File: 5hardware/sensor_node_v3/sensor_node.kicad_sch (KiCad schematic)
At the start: 19 parts, among them J1 Conn_01x15, J2 Conn_01x15, SW2 SW_DIP_x04, SW3 SW_Push, SW5 RotaryEncoder, U5 MCP1700x-330xxTO, U7 CH32V003F4P6

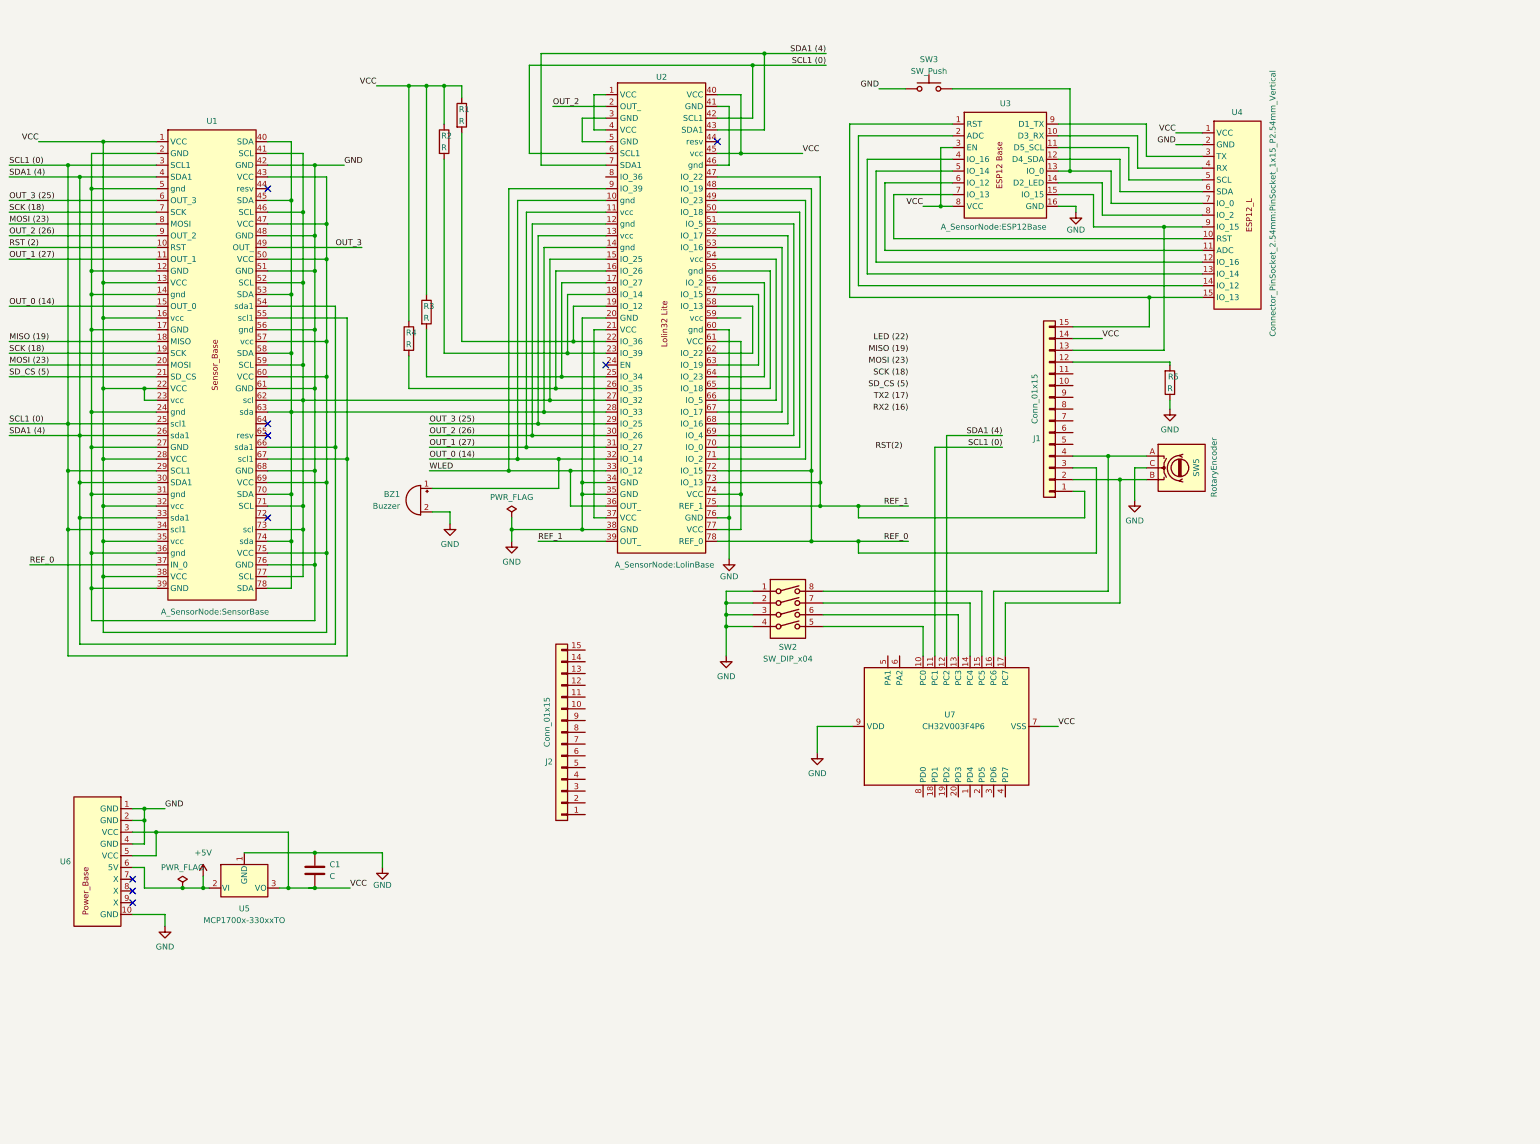
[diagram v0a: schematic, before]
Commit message: updating ESP-Mess baseboard schematic for version 3.0
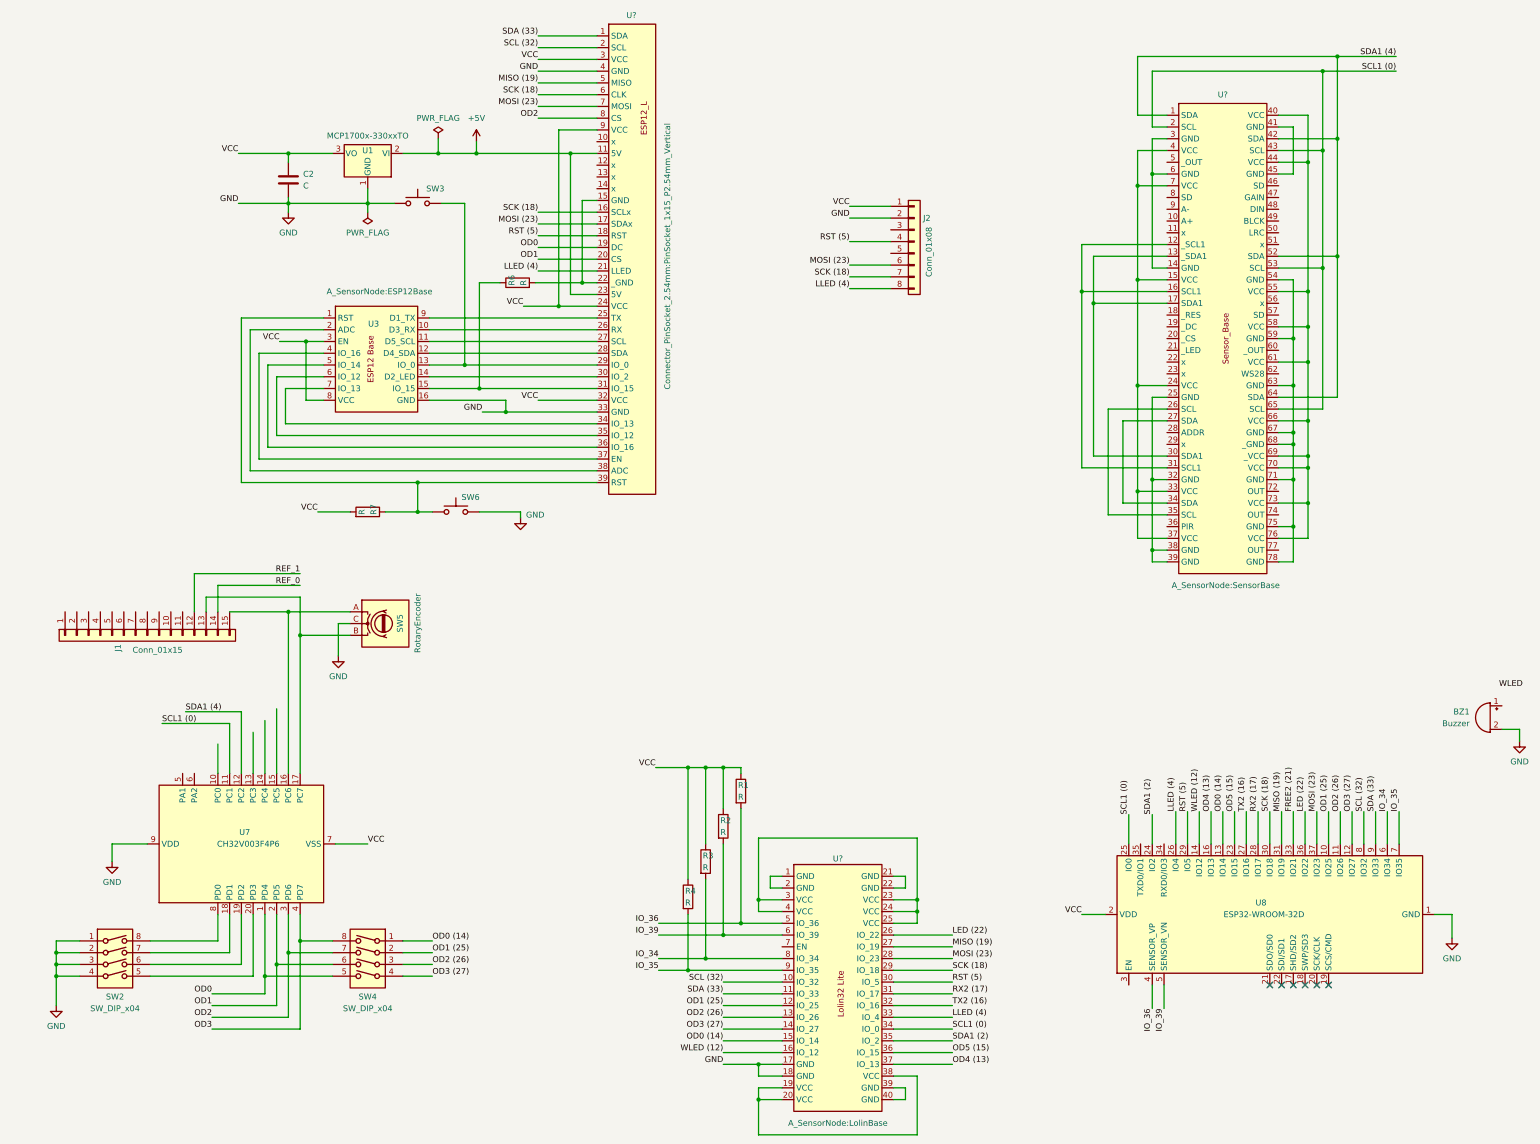
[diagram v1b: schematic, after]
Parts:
- removed C1: C, Capacitor_THT:CP_Radial_D5.0mm_P2.00mm, symbol Device:C
- removed J2: Conn_01x15, symbol Connector_Generic:Conn_01x15
- removed R5: R, Connector_PinSocket_2.54mm:PinSocket_1x02_P2.54mm_Vertical, symbol Device:R
- removed U5: MCP1700x-330xxTO, Package_TO_SOT_THT:TO-92_Inline, symbol Regulator_Linear:MCP1700x-330xxTO
- removed U6: ~, Connector_PinSocket_2.54mm:PinSocket_1x10_P2.54mm_Vertical, symbol A_SensorNode:PowerBase
- added C2: C, Capacitor_THT:CP_Radial_D5.0mm_P2.00mm, symbol Device:C
- added J2: Conn_01x08, symbol Connector_Generic:Conn_01x08
- added R6, R7: R, Connector_PinSocket_2.54mm:PinSocket_1x02_P2.54mm_Vertical, symbol Device:R
- added SW4: SW_DIP_x04, Button_Switch_THT:SW_DIP_SPSTx04_Slide_9.78x12.34mm_W7.62mm_P2.54mm, symbol Switch:SW_DIP_x04
- added SW6: SW_Push, Button_Switch_THT:SW_PUSH_6mm_H7.3mm, symbol Switch:SW_Push
- added U1: MCP1700x-330xxTO, Package_TO_SOT_THT:TO-92_Inline, symbol Regulator_Linear:MCP1700x-330xxTO
- added U8: ESP32-WROOM-32D, RF_Module:ESP32-WROOM-32D, symbol RF_Module:ESP32-WROOM-32D
- renumbered U2 to U?, U4 to U?, U1 to U?
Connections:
- net OUT_2 is gone; now on an unnamed net: U?.2 (GND)
- net +5V: now also U?.11 (5V), U?.23 (5V), U1.2 (VI)
- net GND: now also U?.17 (GND), U?.18 (GND), U?.33 (GND), U?.4 (GND), C2.2, J2.2 (Pin_2), SW6.1, U1.1 (GND), U8.1 (GND), U8.15 (GND), U8.38 (GND), U8.39 (GND); no longer U?.12 (GND), U?.14 (gnd), U?.17 (GND), U?.2 (GND), U?.2 (GND), U?.20 (GND), U?.24 (gnd), U?.27 (GND), U?.31 (gnd), U?.34 (GND), U?.35 (GND), U?.36 (gnd), U?.38 (GND), U?.39 (GND), U?.42 (GND), U?.48 (GND), U?.5 (gnd), U?.51 (GND), U?.56 (gnd), U?.60 (gnd), U?.61 (GND), U?.68 (GND), U?.76 (GND), U?.76 (GND)
- net LED (22): now also U?.26 (IO_22), U8.36 (IO22)
- net MISO (19): now also U?.27 (IO_19), U?.5 (MISO), U8.31 (IO19); no longer U?.18 (MISO)
- net MOSI (23): now also U?.17 (SDAx), U?.28 (IO_23), U?.7 (MOSI), J2.6 (Pin_6), U8.37 (IO23); no longer U?.20 (MOSI), U?.8 (MOSI)
- net REF_0: now also J1.14 (Pin_14); no longer J1.3 (Pin_3), U?.37 (IN_0), U?.48 (IO_19), U?.72 (IO_15), U?.78 (REF_0)
- net REF_1: now also J1.12 (Pin_12); no longer J1.1 (Pin_1), U?.39 (OUT_), U?.47 (IO_22), U?.73 (IO_13), U?.75 (REF_1)
- net SCK (18): now also U?.16 (SCLx), U?.29 (IO_18), U?.6 (CLK), J2.7 (Pin_7), U8.30 (IO18); no longer U?.19 (SCK), U?.7 (SCK)
- net SCL1 (0): now also U?.2 (SCL), U?.34 (IO_0), U?.43 (SCL), U?.53 (SCL), U?.65 (SCL), U8.25 (IO0); no longer U?.25 (scl1), U?.29 (SCL1), U?.3 (SCL1), U?.34 (scl1), U?.42 (SCL1), U?.55 (scl1), U?.6 (SCL1), U?.67 (scl1)
- net SDA1 (4): now also U?.1 (SDA), U?.42 (SDA), U?.52 (SDA), U?.64 (SDA); no longer U?.26 (sda1), U?.30 (SDA1), U?.33 (sda1), U?.4 (SDA1), U?.43 (SDA1), U?.54 (sda1), U?.66 (sda1), U?.7 (SDA1)
- net VCC: now also U?.24 (VCC), U?.3 (VCC), U?.32 (VCC), U?.9 (VCC), C2.1, J2.1 (Pin_1), R7.2, U1.3 (VO), U8.2 (VDD); no longer J1.14 (Pin_14), U?.1 (VCC), U?.1 (VCC), U?.13 (VCC), U?.16 (vcc), U?.22 (VCC), U?.23 (vcc), U?.28 (VCC), U?.32 (vcc), U?.35 (vcc), U?.38 (VCC), U?.40 (VCC), U?.43 (VCC), U?.45 (vcc), U?.47 (VCC), U?.50 (VCC), U?.57 (vcc), U?.60 (VCC), U?.69 (VCC), U?.75 (VCC)
- net WLED: no longer U?.33 (IO_12), U?.36 (OUT_), U?.9 (IO_39)
- net at U?.1 (GND): no longer U?.4 (VCC)
- net at U?.21 (GND): now also U?.22 (GND); no longer U?.37 (VCC)
- net at U?.24 (VCC): now also U?.23 (VCC), U?.25 (VCC), U?.3 (VCC), U?.4 (VCC)
- net IO_36: now reaches U?.5 (IO_36)
- net IO_36: now also R1.2, U8.4 (SENSOR_VP); no longer U?.3 (GND)
- net IO_34: now reaches U?.8 (IO_34)
- net IO_34: now also R3.2, U8.6 (IO34)
- net at SW2.5: now also U7.20 (PD3); no longer U7.10 (PC0)
- net at SW2.6: now also U7.19 (PD2); no longer U7.13 (PC3)
- net at SW2.7: now also U7.18 (PD1); no longer U7.14 (PC4)
- net at SW2.8: now also U7.8 (PD0); no longer U7.15 (PC5)
- net at SW5.A, U7.16 (PC6): now also J1.15 (Pin_15); no longer J1.4 (Pin_4)
- net at SW5.B, U7.17 (PC7): now also J1.13 (Pin_13); no longer J1.2 (Pin_2)
- net at U3.10 (D3_RX): now also U?.26 (RX); no longer U?.4 (RX)
- net at U3.11 (D5_SCL): now also U?.27 (SCL); no longer U?.5 (SCL)
- net at U3.12 (D4_SDA): now also U?.28 (SDA); no longer U?.6 (SDA)
- net at SW3.2, U3.13 (IO_0): now also U?.29 (IO_0); no longer U?.7 (IO_0)
- net at U3.14 (D2_LED): now also U?.30 (IO_2); no longer U?.8 (IO_2)
- net at U3.2 (ADC): now also U?.38 (ADC); no longer U?.14 (IO_12)
- net at U3.4 (IO_16): now also U?.37 (EN); no longer U?.13 (IO_14)
- net at U3.5 (IO_14): now also U?.36 (IO_16); no longer U?.12 (IO_16)
- net at U3.6 (IO_12): now also U?.35 (IO_12); no longer U?.11 (ADC)
- net at U3.7 (IO_13): now also U?.34 (IO_13); no longer U?.10 (RST)
- net at U3.9 (D1_TX): now also U?.25 (TX); no longer U?.3 (TX)
- net OD0: now reaches U7.1 (PD4)
- net OD0: now also U?.19 (DC), SW4.5
- net OD1: now reaches U7.2 (PD5)
- net OD1: now also U?.20 (CS), SW4.6
- net OD2: now reaches U7.3 (PD6)
- net OD2: now also U?.8 (CS), SW4.7
- net OD3: now reaches U7.4 (PD7)
- net OD3: now also SW4.8
- net at U?.44 (VCC): now also U?.40 (VCC), U?.55 (VCC), U?.58 (VCC), U?.61 (VCC), U?.66 (VCC), U?.69 (_VCC), U?.70 (VCC), U?.73 (VCC), U?.76 (VCC)
- removed net OUT_0 (14): BZ1.1 (-), U?.10 (gnd), U?.15 (OUT_0), U?.32 (IO_14)
- removed net OUT_1 (27): U?.11 (OUT_1), U?.11 (vcc), U?.31 (IO_27)
- removed net OUT_2 (26): U?.12 (gnd), U?.30 (IO_26), U?.9 (OUT_2)
- net OUT_3: no longer names the net of U?.49 (BLCK)
- removed net OUT_3 (25): U?.13 (vcc), U?.29 (IO_25), U?.6 (OUT_3)
- net RST (2): no longer names the net of U?.10 (A+)
- net SD_CS (5): no longer names the net of U?.21 (_LED)
- new net: U?.19 (VCC), U?.20 (VCC), U?.38 (VCC)
- new net: U?.39 (GND), U?.40 (GND)
- new net: R7.1, SW6.2, U3.1 (RST), U?.39 (RST)
- new net: R6.1, U3.15 (IO_15), U?.31 (IO_15)
- new net: R6.2, U?.15 (GND), U?.22 (_GND)
- new net: U?.12 (_SCL1), U?.16 (SCL1), U?.31 (SCL1)
- new net: U?.13 (_SDA1), U?.17 (SDA1), U?.30 (SDA1)
- new net: U?.14 (GND), U?.3 (GND), U?.6 (GND)
- new net: U?.15 (VCC), U?.24 (VCC), U?.33 (VCC), U?.37 (VCC), U?.4 (VCC), U?.7 (VCC)
- new net: U?.25 (GND), U?.32 (GND), U?.38 (GND), U?.39 (GND)
- new net: U?.26 (SCL), U?.35 (SCL)
- new net: U?.27 (SDA), U?.34 (SDA)
- new net: U?.41 (GND), U?.45 (GND)
- new net: U?.54 (GND), U?.59 (GND), U?.63 (GND), U?.67 (GND), U?.68 (_GND), U?.71 (GND), U?.75 (GND), U?.78 (GND)
- new net FREE2 (21): U8.33 (IO21)
- new net IO_35: R4.2, U8.7 (IO35), U?.9 (IO_35)
- new net IO_39: R2.2, U8.5 (SENSOR_VN), U?.6 (IO_39)
- new net LLED (4): J2.8 (Pin_8), U8.26 (IO4), U?.21 (LLED), U?.33 (IO_4)
- new net OD0 (14): SW4.1, U8.13 (IO14), U?.15 (IO_14)
- new net OD1 (25): SW4.2, U8.10 (IO25), U?.12 (IO_25)
- new net OD2 (26): SW4.3, U8.11 (IO26), U?.13 (IO_26)
- new net OD3 (27): SW4.4, U8.12 (IO27), U?.14 (IO_27)
- new net OD4 (13): U8.16 (IO13), U?.37 (IO_13)
- new net OD5 (15): U8.23 (IO15), U?.36 (IO_15)
- new net RST (5): J2.4 (Pin_4), U8.29 (IO5), U?.18 (RST), U?.30 (IO_5)
- new net RX2 (17): U8.28 (IO17), U?.31 (IO_17)
- new net SCL (32): U8.8 (IO32), U?.10 (IO_32), U?.2 (SCL)
- new net SDA (33): U8.9 (IO33), U?.1 (SDA), U?.11 (IO_33)
- new net SDA1 (2): U8.24 (IO2), U?.35 (IO_2)
- new net TX2 (16): U8.27 (IO16), U?.32 (IO_16)
- new net WLED (12): U8.14 (IO12), U?.16 (IO_12)
- now unconnected: U?.46 (SCL), U?.62 (scl), U?.74 (sda), U?.77 (SCL)
- no-connect marks 9 -> 6
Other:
- moved on the sheet: BZ1, J1, R1, R2, R3, R4, SW2, SW3, SW5, U3, U7

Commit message: updated schematic.
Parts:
- removed J1: Conn_01x15, symbol Connector_Generic:Conn_01x15
- removed J2: Conn_01x08, symbol Connector_Generic:Conn_01x08
- added J3: Conn_01x29, symbol Connector_Generic:Conn_01x29
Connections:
- net GND: now also R6.2, U?.15 (GND), U?.22 (_GND), J3.2 (Pin_2)
- net LED (22): now also J3.17 (Pin_17)
- net LLED (4): now also J3.8 (Pin_8)
- net MOSI (23): now also J3.6 (Pin_6)
- net OD0: now also BZ1.1 (-)
- net OD0 (14): now also SW4.4; no longer SW4.1
- net OD1 (25): now also SW4.3; no longer SW4.2
- net OD2 (26): now also SW4.2; no longer SW4.3
- net OD3 (27): now also SW4.1; no longer SW4.4
- net OD4 (13): now also J3.28 (Pin_28)
- net OD5 (15): now also J3.26 (Pin_26)
- net RST (5): now also J3.4 (Pin_4)
- net SCK (18): now also J3.7 (Pin_7)
- net SCL1 (0): now also U?.12 (_SCL1), U?.16 (SCL1), U?.31 (SCL1)
- net SDA1 (4): now also U?.13 (_SDA1), U?.17 (SDA1), U?.30 (SDA1)
- net VCC: now also J3.1 (Pin_1)
- net WLED (12): now also J3.18 (Pin_18)
- net at SW5.A, U7.16 (PC6): now also J3.27 (Pin_27)
- net at SW5.B, U7.17 (PC7): now also J3.29 (Pin_29)
- net at U7.10 (PC0): now also J3.22 (Pin_22)
- net at U7.13 (PC3): now also J3.23 (Pin_23)
- net at U7.14 (PC4): now also J3.24 (Pin_24)
- net at U7.15 (PC5): now also J3.25 (Pin_25)
- net at U7.5 (PA1): now also J3.20 (Pin_20)
- net at U7.6 (PA2): now also J3.21 (Pin_21)
- net FREE2 (21) renamed FREE (21)
- net FREE (21): now also J3.19 (Pin_19)
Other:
- moved on the sheet: BZ1, R1, R2, R3, R4, R7, SW2, SW4, SW5, U7, U8, U?

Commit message: schematic draft.
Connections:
- net OD3 (27) is gone; now on net BCLK: SW4.1, U8.12 (IO27), U?.14 (IO_27)
- net IO_34: now also J3.14 (Pin_14)
- net IO_35: now also J3.15 (Pin_15)
- net IO_36: now also J3.12 (Pin_12)
- net IO_39: now also J3.13 (Pin_13)
- net RX: now reaches U8.34 (RXD0/IO3)
- net TX: now reaches U8.35 (TXD0/IO1)
- net BCLK: now reaches J3.16 (Pin_16)
- net BCLK: now also U?.49 (BLCK)
- net AUD0: now reaches U?.5 (_OUT)
- no-connect marks 6 -> 24
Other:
- moved on the sheet: BZ1, C2, J3, R1, R2, R3, R4, R6, R7, SW2, SW3, SW4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

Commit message: label pins.
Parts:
- J3: footprint (none) -> Connector_PinSocket_2.54mm:PinSocket_1x29_P2.54mm_Vertical
- SW2: footprint Button_Switch_THT:SW_DIP_SPSTx04_Slide_9.78x12.34mm_W7.62mm_P2.54mm -> Button_Switch_SMD:SW_DIP_SPSTx04_Slide_6.7x11.72mm_W8.61mm_P2.54mm_LowProfile
- SW4: footprint Button_Switch_THT:SW_DIP_SPSTx04_Slide_9.78x12.34mm_W7.62mm_P2.54mm -> Button_Switch_THT:SW_DIP_SPSTx04_Slide_6.7x11.72mm_W7.62mm_P2.54mm_LowProfile
- U4: renamed from U?; footprint Connector_PinSocket_2.54mm:PinSocket_1x15_P2.54mm_Vertical -> Connector_PinSocket_2.54mm:PinSocket_1x29_P2.54mm_Vertical
- gave numbers to parts that had none: 2
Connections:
- net GND: now also U2.1 (GND), U2.2 (GND), U2.21 (GND), U2.22 (GND), U2.39 (GND), U2.40 (GND), U4.3 (VCC), U5.14 (GND), U5.25 (GND), U5.3 (GND), U5.32 (GND), U5.38 (GND), U5.39 (GND), U5.41 (GND), U5.45 (GND), U5.54 (GND), U5.59 (GND), U5.6 (GND), U5.63 (GND), U5.67 (GND), U5.68 (_GND), U5.71 (GND), U5.75 (GND), U5.78 (GND); no longer U4.4 (GND)
- net IO_39: no longer R2.2, U2.6 (IO_39)
- net MISO (19): now also U4.4 (GND); no longer U4.5 (MISO)
- net SCK (18): now also U4.5 (MISO); no longer U4.6 (CLK)
- net SCL (32): now also U5.26 (SCL), U5.35 (SCL)
- net SDA (33): now also U4.6 (CLK), U5.27 (SDA), U5.34 (SDA)
- net +3.3V: now reaches U2.19 (VCC), U2.20 (VCC), U2.38 (VCC)
- net +3.3V: now also C2.1, J3.1 (Pin_1), R1.1, R2.1, R3.1, R4.1, R7.2, U1.3 (VO), U2.23 (VCC), U2.24 (VCC), U2.25 (VCC), U2.3 (VCC), U2.4 (VCC), U3.3 (EN), U3.8 (VCC), U4.24 (VCC), U4.32 (VCC), U4.9 (VCC), U5.15 (VCC), U5.24 (VCC), U5.33 (VCC), U5.37 (VCC), U5.4 (VCC), U5.40 (VCC), U5.44 (VCC), U5.55 (VCC), U5.58 (VCC), U5.61 (VCC), U5.66 (VCC), U5.69 (_VCC), U5.7 (VCC), U5.70 (VCC), U5.73 (VCC), U5.76 (VCC), U7.7 (VSS), U8.2 (VDD)
- net EN: now reaches U2.7 (EN)
- net EN: now also U8.3 (EN)
- removed net VCC: C2.1, J3.1 (Pin_1), R1.1, R2.1, R3.1, R4.1, R7.2, U1.3 (VO), U3.3 (EN), U3.8 (VCC), U4.24 (VCC), U4.3 (VCC), U4.32 (VCC), U4.9 (VCC), U7.7 (VSS), U8.2 (VDD)
- new net IO_k39: R2.2, U2.6 (IO_39)
- no-connect marks 24 -> 38
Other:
- moved on the sheet: BZ1, C2, J3, R1, R2, R3, R4, R6, R7, SW2, SW3, SW4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
